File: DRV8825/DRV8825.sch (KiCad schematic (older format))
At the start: 15 parts, among them U1 DRV8825PWPR

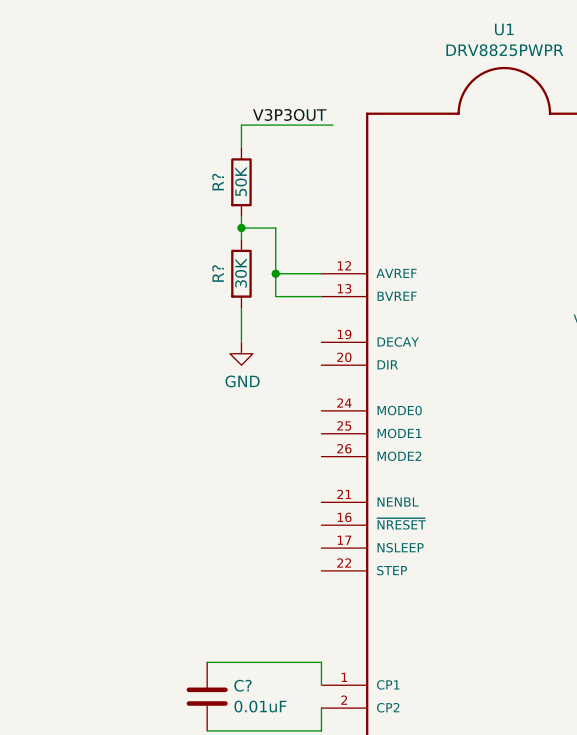
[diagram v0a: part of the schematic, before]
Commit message: FINISH DRV8825
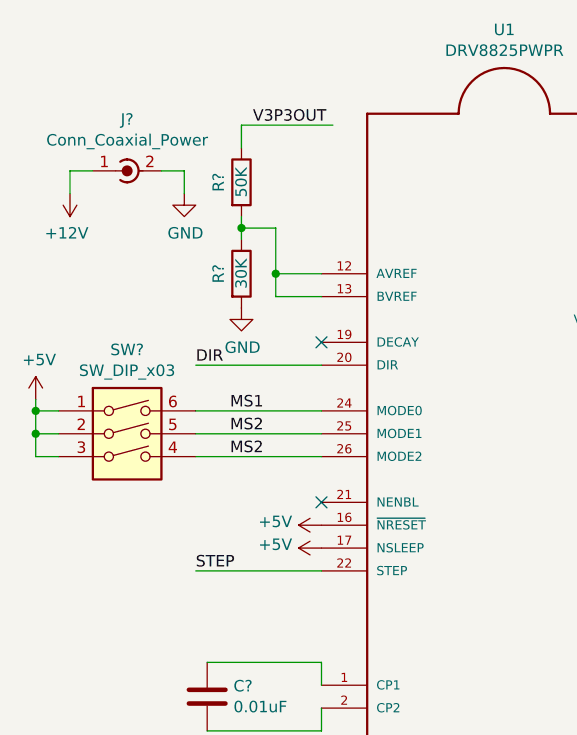
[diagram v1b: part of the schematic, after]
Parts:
- added J?: Conn_Coaxial_Power, Connector_AMASS:AMASS_XT30PW-M_1x02_P2.50mm_Horizontal, symbol Connector:Conn_Coaxial_Power
- added SW?: SW_DIP_x03, Button_Switch_THT:SW_DIP_SPSTx03_Slide_9.78x9.8mm_W7.62mm_P2.54mm, symbol Switch:SW_DIP_x03
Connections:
- net labels added: +5V, DIR, MS1, MS2, STEP
- wire segments 54 -> 68
- no-connect marks 0 -> 2
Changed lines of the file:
@@
 L power:GND #PWR?
 U 1 1 5E5CAE8A
-P 4750 2200
-F 0 "#PWR?" H 4750 1950 50  0001 C CNN
-F 1 "GND" H 4755 2027 50  0000 C CNN
-F 2 "" H 4750 2200 50  0001 C CNN
-F 3 "" H 4750 2200 50  0001 C CNN
-	1    4750 2200
+P 4750 2050
+F 0 "#PWR?" H 4750 1800 50  0001 C CNN
+F 1 "GND" H 4755 1877 50  0000 C CNN
+F 2 "" H 4750 2050 50  0001 C CNN
+F 3 "" H 4750 2050 50  0001 C CNN
+	1    4750 2050
 	1    0    0    -1
 $EndComp
@@
 	4900 1900 4900 2000
 Wire Wire Line
-	4750 2200 4750 2050
-Wire Wire Line
 	4750 1350 4750 1250
 Wire Wire Line
@@
 	0    1    1    0
 $EndComp
+$Comp
+L power:+5V #PWR?
+U 1 1 5E6259D9
+P 5100 3100
+F 0 "#PWR?" H 5100 2950 50  0001 C CNN
+F 1 "+5V" V 5115 3228 50  0000 L CNN
+F 2 "" H 5100 3100 50  0001 C CNN
+F 3 "" H 5100 3100 50  0001 C CNN
+	1    5100 3100
+	0    -1   -1   0
+$EndComp
+$Comp
+L power:+5V #PWR?
+U 1 1 5E627A58
+P 5100 3000
+F 0 "#PWR?" H 5100 2850 50  0001 C CNN
+F 1 "+5V" V 5115 3128 50  0000 L CNN
+F 2 "" H 5100 3000 50  0001 C CNN
+F 3 "" H 5100 3000 50  0001 C CNN
+	1    5100 3000
+	0    -1   -1   0
+$EndComp
+NoConn ~ 5100 2900
+NoConn ~ 5100 2200
+Text Label 4550 2300 0    50   ~ 0
+DIR
+Wire Wire Line
+	5100 2300 4550 2300
+Text Label 4550 3200 0    50   ~ 0
+STEP
+Wire Wire Line
+	5100 3200 4550 3200
+Text Label 4700 2500 0    50   ~ 0
+MS1
+Text Label 4700 2600 0    50   ~ 0
+MS2
+Text Label 4700 2700 0    50   ~ 0
+MS2
+$Comp
+L Switch:SW_DIP_x03 SW?
+U 1 1 5E631C4F
+P 4250 2700
+F 0 "SW?" H 4250 3167 50  0000 C CNN
+F 1 "SW_DIP_x03" H 4250 3076 50  0000 C CNN
+F 2 "Button_Switch_THT:SW_DIP_SPSTx03_Slide_9.78x9.8mm_W7.62mm_P2.54mm" H 4250 2700 50  0001 C CNN
+F 3 "~" H 4250 2700 50  0001 C CNN
+	1    4250 2700
+	1    0    0    -1
+$EndComp
+$Comp
+L power:+5V #PWR?
+U 1 1 5E634C75
+P 3850 2450
+F 0 "#PWR?" H 3850 2300 50  0001 C CNN
+F 1 "+5V" H 3865 2623 50  0000 C CNN
+F 2 "" H 3850 2450 50  0001 C CNN
+F 3 "" H 3850 2450 50  0001 C CNN
+	1    3850 2450
+	1    0    0    -1
+$EndComp
+Wire Wire Line
+	3850 2450 3850 2500
+Wire Wire Line
+	3850 2700 3950 2700
+Wire Wire Line
+	3950 2600 3850 2600
+Connection ~ 3850 2600
+Wire Wire Line
+	3850 2600 3850 2700
+Wire Wire Line
+	3950 2500 3850 2500
+Connection ~ 3850 2500
+Wire Wire Line
+	3850 2500 3850 2600
+Wire Wire Line
+	4550 2500 5100 2500
+Wire Wire Line
+	4550 2600 5100 2600
+Wire Wire Line
+	4550 2700 5100 2700
+$Comp
+L Connector:Conn_Coaxial_Power J?
+U 1 1 5E63E330
+P 4200 1450
+F 0 "J?" V 4425 1400 50  0000 C CNN
+F 1 "Conn_Coaxial_Power" V 4334 1400 50  0000 C CNN
+F 2 "Connector_AMASS:AMASS_XT30PW-M_1x02_P2.50mm_Horizontal" H 4200 1400 50  0001 C CNN
+F 3 "~" H 4200 1400 50  0001 C CNN
+	1    4200 1450
+	0    -1   -1   0
+$EndComp
+$Comp
+L power:GND #PWR?
+U 1 1 5E644E90
+P 4500 1550
+F 0 "#PWR?" H 4500 1300 50  0001 C CNN
+F 1 "GND" H 4505 1377 50  0000 C CNN
+F 2 "" H 4500 1550 50  0001 C CNN
+F 3 "" H 4500 1550 50  0001 C CNN
+	1    4500 1550
+	1    0    0    -1
+$EndComp
+$Comp
+L power:+12V #PWR?
+U 1 1 5E647686
+P 4000 1550
+F 0 "#PWR?" H 4000 1400 50  0001 C CNN
+F 1 "+12V" H 4015 1723 50  0000 C CNN
+F 2 "" H 4000 1550 50  0001 C CNN
+F 3 "" H 4000 1550 50  0001 C CNN
+	1    4000 1550
+	-1   0    0    1
+$EndComp
+Wire Wire Line
+	4400 1450 4500 1450
+Wire Wire Line
+	4500 1450 4500 1550
+Wire Wire Line
+	4100 1450 4000 1450
+Wire Wire Line
+	4000 1450 4000 1550
 $EndSCHEMATC

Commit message: FINISH AGAIN
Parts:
- gave numbers to parts that had none: 14
- renumbered C-VMA to C-VMA1, C-VMB to C-VMB1
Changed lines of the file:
@@
 $EndComp
 $Comp
-L power:GND #PWR?
+L power:GND #PWR0101
 U 1 1 5E5CA1CC
 P 6700 4800
-F 0 "#PWR?" H 6700 4550 50  0001 C CNN
+F 0 "#PWR0101" H 6700 4550 50  0001 C CNN
 F 1 "GND" H 6705 4627 50  0000 C CNN
 F 2 "" H 6700 4800 50  0001 C CNN
@@
 $EndComp
 $Comp
-L power:GND #PWR?
+L power:GND #PWR0102
 U 1 1 5E5CAE8A
 P 4750 2050
-F 0 "#PWR?" H 4750 1800 50  0001 C CNN
+F 0 "#PWR0102" H 4750 1800 50  0001 C CNN
 F 1 "GND" H 4755 1877 50  0000 C CNN
 F 2 "" H 4750 2050 50  0001 C CNN
@@
 $EndComp
 $Comp
-L Device:R R?
+L Device:R R1
 U 1 1 5E5CB7B2
 P 4300 4150
-F 0 "R?" H 4370 4196 50  0000 L CNN
+F 0 "R1" H 4370 4196 50  0000 L CNN
 F 1 "1M" H 4370 4105 50  0000 L CNN
 F 2 "Resistor_SMD:R_0603_1608Metric_Pad1.05x0.95mm_HandSolder" V 4230 4150 50  0001 C CNN
@@
 $EndComp
 $Comp
-L Device:C C?
+L Device:C C3
 U 1 1 5E5D2788
 P 6700 1950
-F 0 "C?" H 6815 1996 50  0000 L CNN
+F 0 "C3" H 6815 1996 50  0000 L CNN
 F 1 "0.47uF" H 6815 1905 50  0000 L CNN
 F 2 "Capacitor_SMD:C_0201_0603Metric" H 6738 1800 50  0001 C CNN
@@
 $EndComp
 $Comp
-L power:+12V #PWR?
+L power:+12V #PWR0103
 U 1 1 5E5D55F9
 P 6700 1300
-F 0 "#PWR?" H 6700 1150 50  0001 C CNN
+F 0 "#PWR0103" H 6700 1150 50  0001 C CNN
 F 1 "+12V" H 6715 1473 50  0000 C CNN
 F 2 "" H 6700 1300 50  0001 C CNN
@@
 Connection ~ 6700 1300
 $Comp
-L Device:C C?
+L Device:C C2
 U 1 1 5E5DA2EF
 P 4600 4150
-F 0 "C?" H 4715 4196 50  0000 L CNN
+F 0 "C2" H 4715 4196 50  0000 L CNN
 F 1 "0.1uF" H 4715 4105 50  0000 L CNN
 F 2 "Capacitor_SMD:C_0201_0603Metric" H 4638 4000 50  0001 C CNN
@@
 $EndComp
 $Comp
-L power:+12V #PWR?
+L power:+12V #PWR0104
 U 1 1 5E5E3FD3
 P 4600 4450
-F 0 "#PWR?" H 4600 4300 50  0001 C CNN
+F 0 "#PWR0104" H 4600 4300 50  0001 C CNN
 F 1 "+12V" H 4615 4623 50  0000 C CNN
 F 2 "" H 4600 4450 50  0001 C CNN
@@
 Connection ~ 4600 4400
 $Comp
-L Device:C C?
+L Device:C C1
 U 1 1 5E5E742C
 P 4600 3750
-F 0 "C?" H 4715 3796 50  0000 L CNN
+F 0 "C1" H 4715 3796 50  0000 L CNN
 F 1 "0.01uF" H 4715 3705 50  0000 L CNN
 F 2 "Capacitor_SMD:C_0201_0603Metric" H 4638 3600 50  0001 C CNN
@@
 	5100 3900 4600 3900
 $Comp
-L Device:R R?
+L Device:R R4
 U 1 1 5E5E8AA0
 P 4850 4650
-F 0 "R?" H 4920 4696 50  0000 L CNN
+F 0 "R4" H 4920 4696 50  0000 L CNN
 F 1 "200m" V 4850 4550 50  0000 L CNN
 F 2 "Resistor_SMD:R_0603_1608Metric_Pad1.05x0.95mm_HandSolder" V 4780 4650 50  0001 C CNN
@@
 	4850 4200 4850 4500
 $Comp
-L Device:R R?
+L Device:R R5
 U 1 1 5E5EA247
 P 5100 4650
-F 0 "R?" H 5170 4696 50  0000 L CNN
+F 0 "R5" H 5170 4696 50  0000 L CNN
 F 1 "200m" V 5100 4550 50  0000 L CNN
 F 2 "Resistor_SMD:R_0603_1608Metric_Pad1.05x0.95mm_HandSolder" V 5030 4650 50  0001 C CNN
@@
 	5100 4300 5100 4500
 $Comp
-L power:GND #PWR?
+L power:GND #PWR0105
 U 1 1 5E5EAA71
 P 5100 4800
-F 0 "#PWR?" H 5100 4550 50  0001 C CNN
+F 0 "#PWR0105" H 5100 4550 50  0001 C CNN
 F 1 "GND" H 5105 4627 50  0000 C CNN
 F 2 "" H 5100 4800 50  0001 C CNN
@@
 $EndComp
 $Comp
-L power:GND #PWR?
+L power:GND #PWR0106
 U 1 1 5E5EB3DF
 P 4850 4800
-F 0 "#PWR?" H 4850 4550 50  0001 C CNN
+F 0 "#PWR0106" H 4850 4550 50  0001 C CNN
 F 1 "GND" H 4855 4627 50  0000 C CNN
 F 2 "" H 4850 4800 50  0001 C CNN
@@
 V3P3OUT
 $Comp
-L power:GND #PWR?
+L power:GND #PWR0107
 U 1 1 5E5EC6B8
 P 6700 1800
-F 0 "#PWR?" H 6700 1550 50  0001 C CNN
+F 0 "#PWR0107" H 6700 1550 50  0001 C CNN
 F 1 "GND" H 6705 1627 50  0000 C CNN
 F 2 "" H 6700 1800 50  0001 C CNN
@@
 $EndComp
 $Comp
-L Device:R R?
+L Device:R R6
 U 1 1 5E5EE5E6
 P 6850 2300
-F 0 "R?" V 6950 2300 50  0000 C CNN
+F 0 "R6" V 6950 2300 50  0000 C CNN
 F 1 "10K" V 6850 2300 50  0000 C CNN
 F 2 "Resistor_SMD:R_0603_1608Metric_Pad1.05x0.95mm_HandSolder" V 6780 2300 50  0001 C CNN
@@
 $EndComp
 $Comp
-L Device:R R?
+L Device:R R7
 U 1 1 5E5F31A6
 P 6850 2400
-F 0 "R?" V 6750 2400 50  0000 C CNN
+F 0 "R7" V 6750 2400 50  0000 C CNN
 F 1 "10K" V 6850 2400 50  0000 C CNN
 F 2 "Resistor_SMD:R_0603_1608Metric_Pad1.05x0.95mm_HandSolder" V 6780 2400 50  0001 C CNN
@@
 Connection ~ 7100 2300
 $Comp
-L Device:CP CP?
+L Device:CP CP1
 U 1 1 5E5F5161
 P 6950 1350
-F 0 "CP?" V 6695 1350 50  0000 C CNN
+F 0 "CP1" V 6695 1350 50  0000 C CNN
 F 1 "100uF" V 6786 1350 50  0000 C CNN
 F 2 "Capacitor_Tantalum_SMD:CP_EIA-1608-08_AVX-J" H 6988 1200 50  0001 C CNN
@@
 	6700 1350 6700 1400
 $Comp
-L power:GND #PWR?
+L power:GND #PWR0108
 U 1 1 5E5F8916
 P 7150 1400
-F 0 "#PWR?" H 7150 1150 50  0001 C CNN
+F 0 "#PWR0108" H 7150 1150 50  0001 C CNN
 F 1 "GND" H 7155 1227 50  0000 C CNN
 F 2 "" H 7150 1400 50  0001 C CNN
@@
 	7150 1350 7150 1400
 $Comp
-L Device:R R?
+L Device:R R2
 U 1 1 5E5FA975
 P 4750 1500
-F 0 "R?" V 4650 1500 50  0000 C CNN
+F 0 "R2" V 4650 1500 50  0000 C CNN
 F 1 "50K" V 4750 1500 50  0000 C CNN
 F 2 "Resistor_SMD:R_0603_1608Metric_Pad1.05x0.95mm_HandSolder" V 4680 1500 50  0001 C CNN
@@
 $EndComp
 $Comp
-L Device:R R?
+L Device:R R3
 U 1 1 5E5FD16F
 P 4750 1900
-F 0 "R?" V 4650 1900 50  0000 C CNN
+F 0 "R3" V 4650 1900 50  0000 C CNN
 F 1 "30K" V 4750 1900 50  0000 C CNN
 F 2 "Resistor_SMD:R_0603_1608Metric_Pad1.05x0.95mm_HandSolder" V 4680 1900 50  0001 C CNN
@@
 V3P3OUT
 $Comp
-L Connector:Conn_01x04_Male J?
+L Connector:Conn_01x04_Male J2
 U 1 1 5E60B6B4
 P 7100 2850
-F 0 "J?" H 7072 2732 50  0000 R CNN
+F 0 "J2" H 7072 2732 50  0000 R CNN
 F 1 "Conn_01x04_Male" H 7072 2823 50  0000 R CNN
 F 2 "Connector_Molex:Molex_PicoBlade_53047-0410_1x04_P1.25mm_Vertical" H 7100 2850 50  0001 C CNN
@@
 	6800 3000 6700 3000
 $Comp
-L Device:C C-VMA
+L Device:C C-VMA1
 U 1 1 5E6128D6
 P 6800 3550
-F 0 "C-VMA" V 6548 3550 50  0000 C CNN
+F 0 "C-VMA1" V 6548 3550 50  0000 C CNN
 F 1 "0.1uF" V 6639 3550 50  0000 C CNN
 F 2 "Capacitor_SMD:C_0201_0603Metric" H 6838 3400 50  0001 C CNN
@@
 $EndComp
 $Comp
-L power:+12V #PWR?
+L power:+12V #PWR0109
 U 1 1 5E61EB61
 P 6600 3350
-F 0 "#PWR?" H 6600 3200 50  0001 C CNN
+F 0 "#PWR0109" H 6600 3200 50  0001 C CNN
 F 1 "+12V" H 6615 3523 50  0000 C CNN
 F 2 "" H 6600 3350 50  0001 C CNN
@@
 $EndComp
 $Comp
-L power:GND #PWR?
+L power:GND #PWR0110
 U 1 1 5E61FED4
 P 7000 4150
-F 0 "#PWR?" H 7000 3900 50  0001 C CNN
+F 0 "#PWR0110" H 7000 3900 50  0001 C CNN
 F 1 "GND" H 7005 3977 50  0000 C CNN
 F 2 "" H 7000 4150 50  0001 C CNN
@@
 	7000 4000 7000 4150
 $Comp
-L Device:C C-VMB
+L Device:C C-VMB1
 U 1 1 5E61E3FE
 P 6800 4000
-F 0 "C-VMB" V 6548 4000 50  0000 C CNN
+F 0 "C-VMB1" V 6548 4000 50  0000 C CNN
 F 1 "0.1uF" V 6639 4000 50  0000 C CNN
 F 2 "Capacitor_SMD:C_0201_0603Metric" H 6838 3850 50  0001 C CNN
@@
 $EndComp
 $Comp
-L power:+5V #PWR?
+L power:+5V #PWR0111
 U 1 1 5E6259D9
 P 5100 3100
-F 0 "#PWR?" H 5100 2950 50  0001 C CNN
+F 0 "#PWR0111" H 5100 2950 50  0001 C CNN
 F 1 "+5V" V 5115 3228 50  0000 L CNN
 F 2 "" H 5100 3100 50  0001 C CNN
@@
 $EndComp
 $Comp
-L power:+5V #PWR?
+L power:+5V #PWR0112
 U 1 1 5E627A58
 P 5100 3000
-F 0 "#PWR?" H 5100 2850 50  0001 C CNN
+F 0 "#PWR0112" H 5100 2850 50  0001 C CNN
 F 1 "+5V" V 5115 3128 50  0000 L CNN
 F 2 "" H 5100 3000 50  0001 C CNN
@@
 MS2
 $Comp
-L Switch:SW_DIP_x03 SW?
+L Switch:SW_DIP_x03 SW1
 U 1 1 5E631C4F
 P 4250 2700
-F 0 "SW?" H 4250 3167 50  0000 C CNN
+F 0 "SW1" H 4250 3167 50  0000 C CNN
 F 1 "SW_DIP_x03" H 4250 3076 50  0000 C CNN
 F 2 "Button_Switch_THT:SW_DIP_SPSTx03_Slide_9.78x9.8mm_W7.62mm_P2.54mm" H 4250 2700 50  0001 C CNN
@@
 $EndComp
 $Comp
-L power:+5V #PWR?
+L power:+5V #PWR0113
 U 1 1 5E634C75
 P 3850 2450
-F 0 "#PWR?" H 3850 2300 50  0001 C CNN
+F 0 "#PWR0113" H 3850 2300 50  0001 C CNN
 F 1 "+5V" H 3865 2623 50  0000 C CNN
 F 2 "" H 3850 2450 50  0001 C CNN
@@
 	4550 2700 5100 2700
 $Comp
-L Connector:Conn_Coaxial_Power J?
+L Connector:Conn_Coaxial_Power J1
 U 1 1 5E63E330
 P 4200 1450
-F 0 "J?" V 4425 1400 50  0000 C CNN
+F 0 "J1" V 4425 1400 50  0000 C CNN
 F 1 "Conn_Coaxial_Power" V 4334 1400 50  0000 C CNN
 F 2 "Connector_AMASS:AMASS_XT30PW-M_1x02_P2.50mm_Horizontal" H 4200 1400 50  0001 C CNN
@@
 $EndComp
 $Comp
-L power:GND #PWR?
+L power:GND #PWR0114
 U 1 1 5E644E90
 P 4500 1550
-F 0 "#PWR?" H 4500 1300 50  0001 C CNN
+F 0 "#PWR0114" H 4500 1300 50  0001 C CNN
 F 1 "GND" H 4505 1377 50  0000 C CNN
 F 2 "" H 4500 1550 50  0001 C CNN
@@
 $EndComp
 $Comp
-L power:+12V #PWR?
+L power:+12V #PWR0115
 U 1 1 5E647686
 P 4000 1550
-F 0 "#PWR?" H 4000 1400 50  0001 C CNN
+F 0 "#PWR0115" H 4000 1400 50  0001 C CNN
 F 1 "+12V" H 4015 1723 50  0000 C CNN
 F 2 "" H 4000 1550 50  0001 C CNN
